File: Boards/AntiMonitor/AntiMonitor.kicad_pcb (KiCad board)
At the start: 2 copper layers, 96.5 x 76.2 mm, 19 parts, among them J1 Data Bus, J2 Address Bus, J3 PWR, J4 System Bus, SW1 SW_SPDT, SW2 RESET, U1 74LS299, U2 74LS299, U3 74LS299

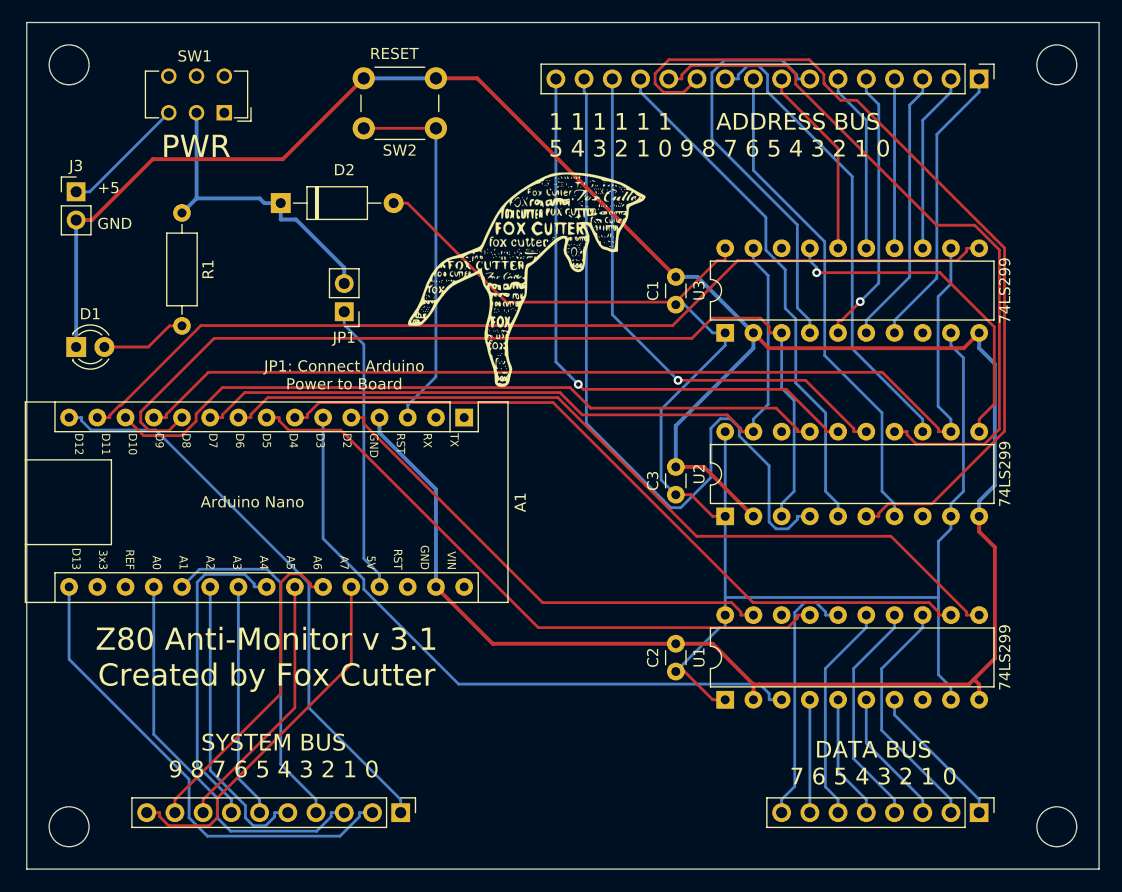
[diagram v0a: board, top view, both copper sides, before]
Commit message: * Antimonitor board update * INT controller tweaks * Opcode XML adjusted slightly * Table builder to output C++ EMU tables * ZASM updates
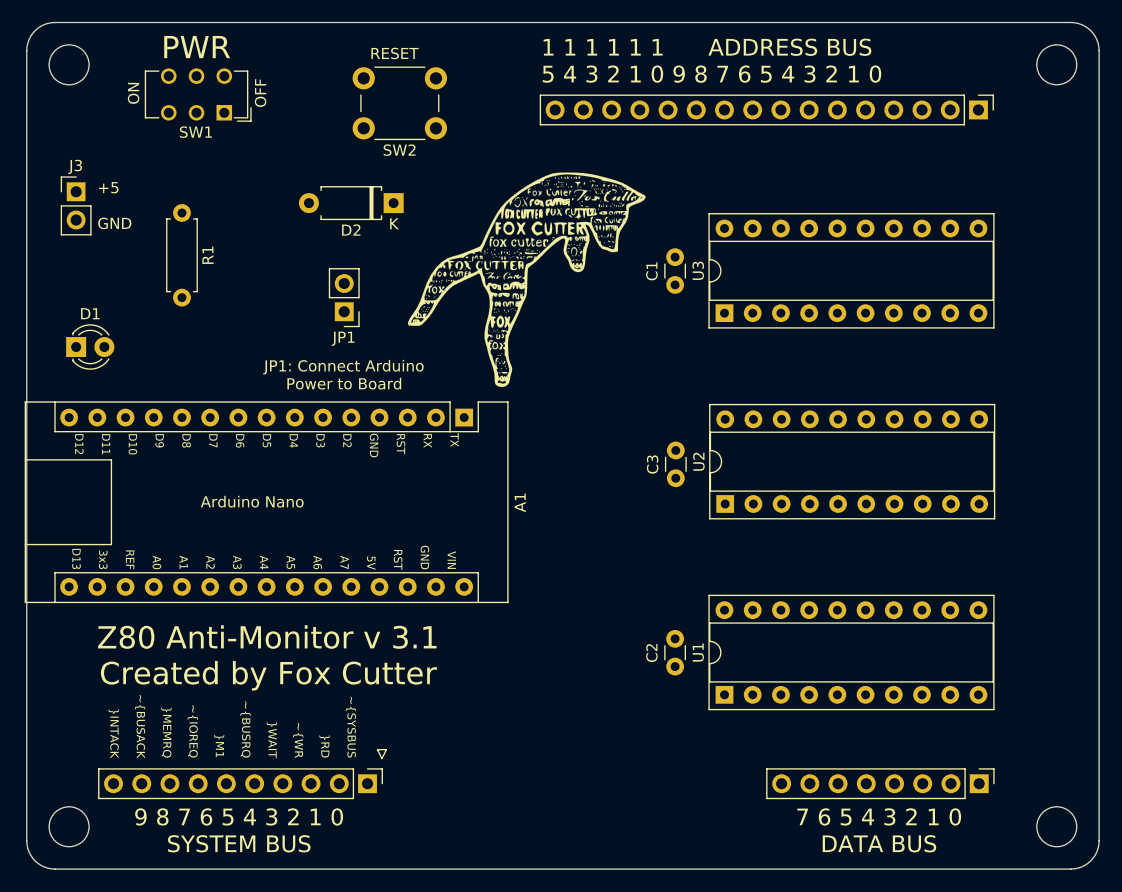
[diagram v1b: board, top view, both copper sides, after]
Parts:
- removed REF**: OSHW-Logo2_14.6x12mm_SilkScreen, Symbol:OSHW-Logo2_14.6x12mm_SilkScreen
- D2: value DIODE -> D_ALT; footprint Diode_THT:D_A-405_P10.16mm_Horizontal -> Diode_THT:D_A-405_P7.62mm_Horizontal
- R1: footprint Resistor_THT:R_Axial_DIN0207_L6.3mm_D2.5mm_P10.16mm_Horizontal -> Resistor_THT:R_Axial_DIN0207_L6.3mm_D2.5mm_P7.62mm_Horizontal
- U1, U2, U3: footprint Package_DIP:DIP-20_W7.62mm -> Package_DIP:DIP-20_W7.62mm_Socket
- moved D2 10.2 mm to (139.7, 80.8), turned to 180 degrees
- moved J4 3.96 mm to (137.4, 133.0)
- moved J2 2.79 mm to (192.3, 72.4)
- moved J1 2.60 mm to (192.4, 133.0)
- moved U3 1.78 mm to (169.5, 90.7)
- moved C1 1.78 mm to (165.0, 88.1)
- moved C3 1.48 mm to (165.1, 105.5)
- moved U2 1.11 mm to (169.5, 107.9)
- moved C2 0.45 mm to (165.0, 122.5)
- moved U1 0.45 mm to (169.5, 125.0)
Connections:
- A1 pad 1: Net-(A1-Pad1) -> (no net)
- A1 pad 17: Net-(A1-Pad17) -> (no net)
- A1 pad 18: Net-(A1-Pad18) -> (no net)
- A1 pad 2: Net-(A1-Pad2) -> (no net)
- A1 pad 3: Net-(A1-Pad3) -> Net-(A1-Pad28)
- A1 pad 30: Net-(A1-Pad30) -> (no net)
- D2 pad 1: +5V -> VCC
- D2 pad 2: VCC -> Net-(D2-Pad2)
- JP1 pad 2: +5V -> Net-(D2-Pad2)
- R1 pad 1: +5V -> Net-(D2-Pad2)
- SW1 pad 1: Net-(SW1-Pad1) -> (no net)
- SW1 pad 2: +5V -> Net-(D2-Pad2)
- SW2 pad 1: Net-(A1-Pad3) -> Net-(SW2-Pad1)
- U1 pad 18: Net-(U1-Pad18) -> (no net)
- U1 pad 8: Net-(U1-Pad8) -> (no net)
- U2 pad 18: Net-(U2-Pad18) -> (no net)
- U2 pad 8: Net-(U2-Pad8) -> (no net)
- U3 pad 18: Net-(U3-Pad18) -> (no net)
- U3 pad 8: Net-(U3-Pad8) -> (no net)
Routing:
- net GND: track 239.1 -> 0.00 mm
- net VCC: track 148.0 -> 0.00 mm
- net Net-(A1-Pad12): track 93.5 -> 0.00 mm
- net Net-(A1-Pad14): track 86.0 -> 0.00 mm
- net Net-(A1-Pad11): track 84.9 -> 0.00 mm
- net Net-(J2-Pad11): track 77.3 -> 0.00 mm
- net Net-(A1-Pad9): track 75.9 -> 0.00 mm
- net Net-(A1-Pad10): track 69.2 -> 0.00 mm
- net Net-(J2-Pad15): track 68.4 -> 0.00 mm
- net Net-(A1-Pad7): track 67.9 -> 0.00 mm
- net Net-(A1-Pad13): track 66.2 -> 0.00 mm
- net Net-(J2-Pad12): track 64.6 -> 0.00 mm
- net Net-(A1-Pad6): track 59.0 -> 0.00 mm
- net Net-(A1-Pad8): track 57.5 -> 0.00 mm
- net Net-(J2-Pad16): track 53.6 -> 0.00 mm, vias 1 -> 0
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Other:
- outline, holes or cut-outs redrawn
- board text added: "7 6 5 4 3 2 1 0 DATA BUS"
- board text added: "9 8 7 6 5 4 3 2 1 0 SYSTEM BUS"
- board text added: "OFF"
- board text added: "ON"
- board text added: "~SYSBUS ~RD ~WR ~WAIT ~BUSRQ ~M1 ~IOREQ ~MEMRQ ~BUSACK ~INTACK"
- board text removed: "DATA BUS 7 6 5 4 3 2 1 0"
- board text removed: "SYSTEM BUS 9 8 7 6 5 4 3 2 1 0"
